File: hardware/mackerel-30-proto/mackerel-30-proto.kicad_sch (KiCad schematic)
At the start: 38 parts, among them J1 Conn_01x02, J2 Conn_01x02, J3 Conn_02x05_Odd_Even, U1 MC68030RC, U2 EPM7128, X1 CXO_DIP14

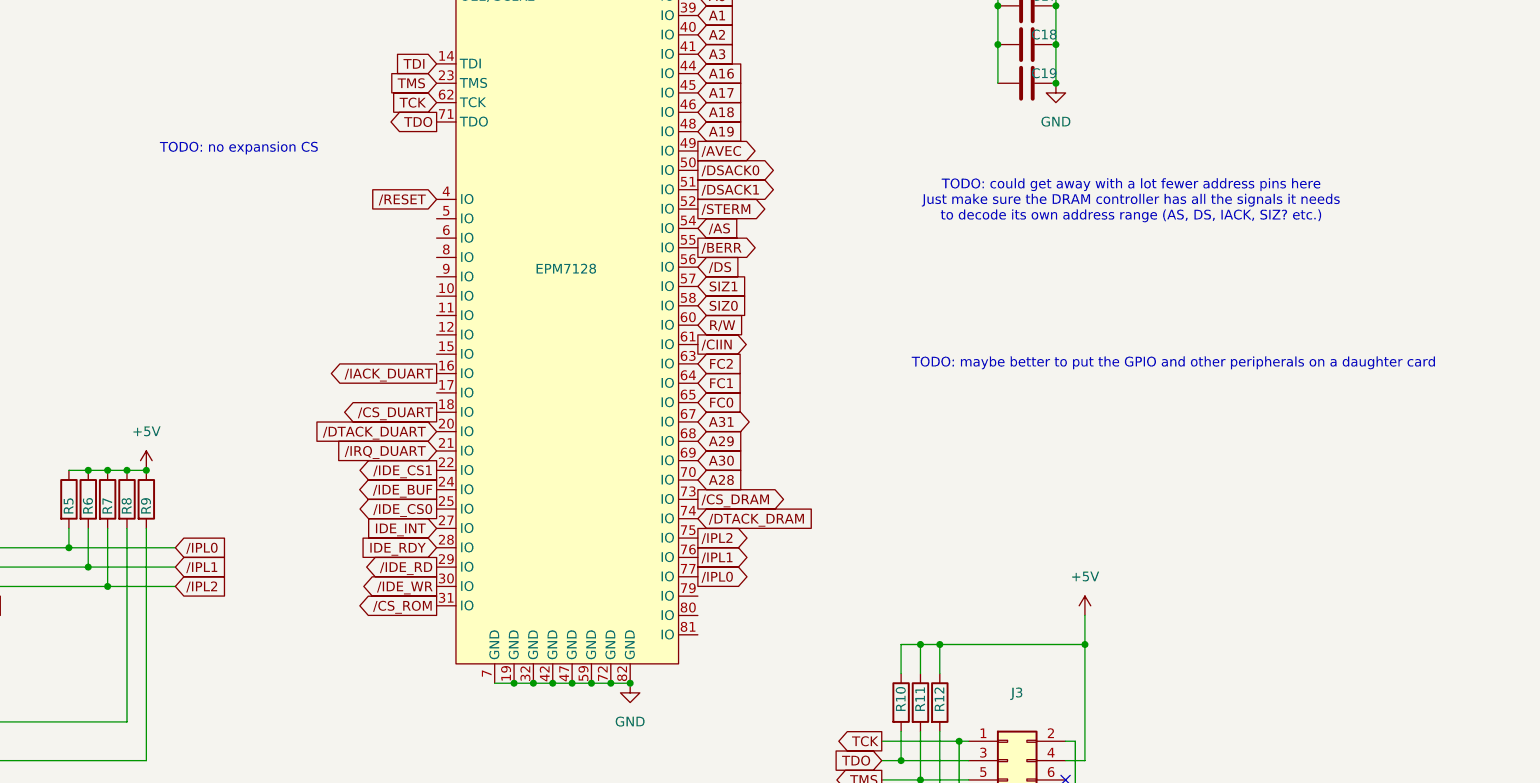
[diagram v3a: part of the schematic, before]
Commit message: Expansion header routed
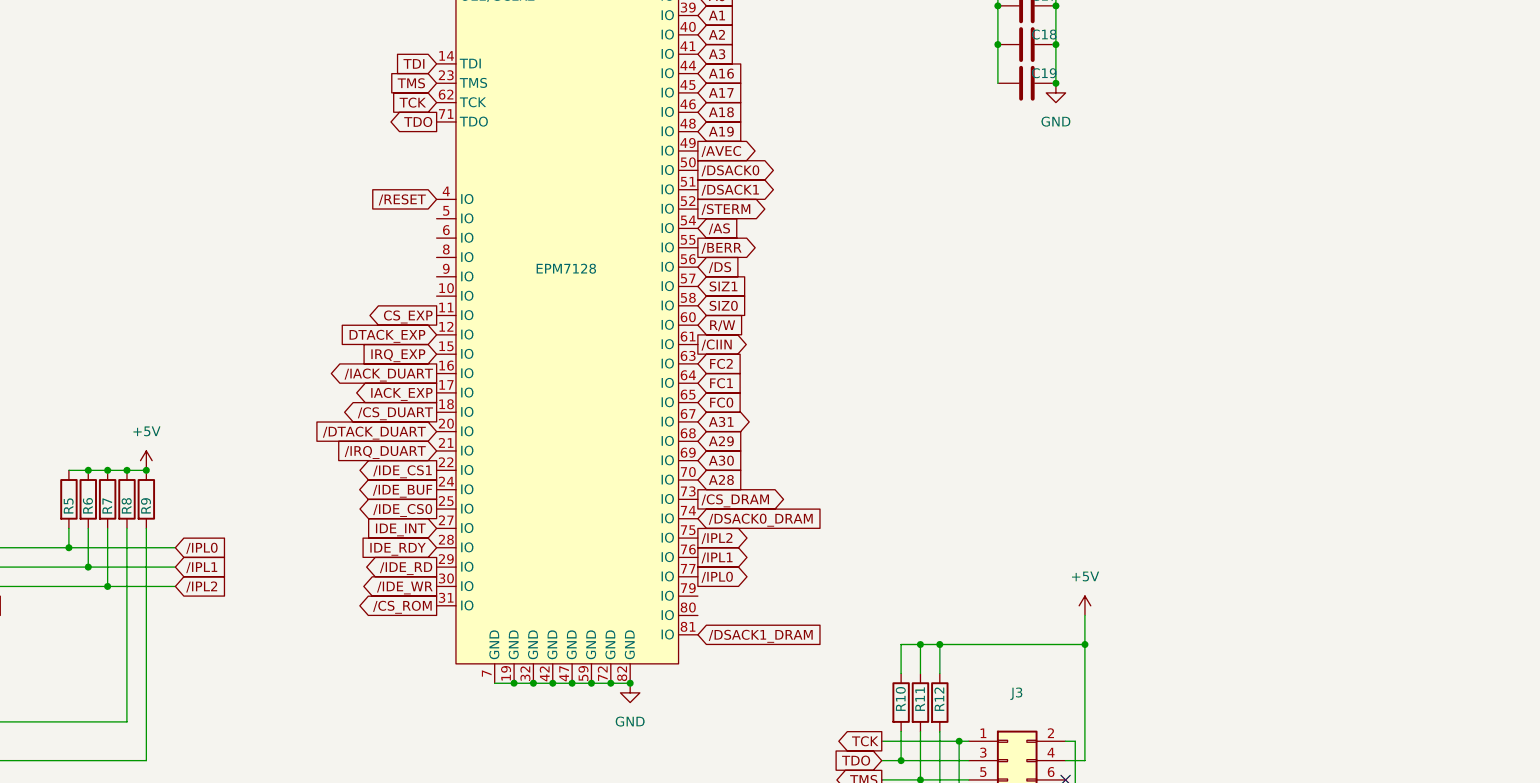
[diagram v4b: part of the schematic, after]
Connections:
- net CS_EXP: now reaches U2.11 (IO)
- net DTACK_EXP: now reaches U2.12 (IO)
- net IRQ_EXP: now reaches U2.15 (IO)
- net IACK_EXP: now reaches U2.17 (IO)
- net /DSACK1_DRAM: now reaches U2.81 (IO)
- net /DTACK_DRAM renamed /DSACK0_DRAM
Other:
- note removed: "TODO: could get away with a lot fewer address pins here Just make sure the DRAM controller has all the signals it needs to decode its own address range (AS, DS, IACK, SIZ? etc.)"
- note removed: "TODO: maybe better to put the GPIO and other peripherals on a daughter card"
- note removed: "TODO: no expansion CS"
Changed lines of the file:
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@@
-		)
-	)
-	(text "TODO: maybe better to put the GPIO and other peripherals on a daughter card"
-		(exclude_from_sim no)
-		(at 274.574 95.25 0)
-		(effects
-			(font
-				(size 1.27 1.27)
-			)
-		)
-	)
-	(text "TODO: no expansion CS"
-		(exclude_from_sim no)
-		(at 151.892 67.056 0)
-		(effects
-			(font
-				(size 1.27 1.27)
-			)
-		)
-	)
-	(text "TODO: could get away with a lot fewer address pins here\nJust make sure the DRAM controller has all the signals it needs\nto decode its own address range (AS, DS, IACK, SIZ? etc.)"
-		(exclude_from_sim no)
-		(at 268.986 73.914 0)
-		(effects
-			(font
-				(size 1.27 1.27)
-			)
 		)
 	)
@@
 		)
 	)
+	(global_label "{slash}DSACK1_DRAM"
+		(shape input)
+		(at 212.09 130.81 0)
+		(fields_autoplaced yes)
+		(effects
+			(font
+				(size 1.27 1.27)
+			)
+			(justify left)
+		)
+		(property "Intersheetrefs" "${INTERSHEET_REFS}"
+			(at 229.7709 130.81 0)
+			(effects
+				(font
+					(size 1.27 1.27)
+				)
+				(justify left)
+				(hide yes)
+			)
+		)
+	)
 	(global_label "{slash}IPL0"
 		(shape output)
@@
 		)
 	)
+	(global_label "DTACK_EXP"
+		(shape input)
+		(at 177.8 91.44 180)
+		(fields_autoplaced yes)
+		(effects
+			(font
+				(size 1.27 1.27)
+			)
+			(justify right)
+		)
+		(property "Intersheetrefs" "${INTERSHEET_REFS}"
+			(at 164.3525 91.44 0)
+			(effects
+				(font
+					(size 1.27 1.27)
+				)
+				(justify right)
+				(hide yes)
+			)
+		)
+	)
 	(global_label "{slash}CS_ROM"
 		(shape output)
@@
 		)
 	)
+	(global_label "IRQ_EXP"
+		(shape input)
+		(at 177.8 93.98 180)
+		(fields_autoplaced yes)
+		(effects
+			(font
+				(size 1.27 1.27)
+			)
+			(justify right)
+		)
+		(property "Intersheetrefs" "${INTERSHEET_REFS}"
+			(at 167.0134 93.98 0)
+			(effects
+				(font
+					(size 1.27 1.27)
+				)
+				(justify right)
+				(hide yes)
+			)
+		)
+	)
 	(global_label "FC2"
 		(shape output)
@@
 		)
 	)
-	(global_label "{slash}DTACK_DRAM"
+	(global_label "{slash}DSACK0_DRAM"
 		(shape input)
 		(at 212.09 115.57 0)
@@
 		)
 		(property "Intersheetrefs" "${INTERSHEET_REFS}"
-			(at 228.3195 115.57 0)
+			(at 229.7709 115.57 0)
 			(effects
 				(font
@@
 		)
 	)
+	(global_label "IACK_EXP"
+		(shape output)
+		(at 177.8 99.06 180)
+		(fields_autoplaced yes)
+		(effects
+			(font
+				(size 1.27 1.27)
+			)
+			(justify right)
+		)
+		(property "Intersheetrefs" "${INTERSHEET_REFS}"
+			(at 165.9853 99.06 0)
+			(effects
+				(font
+					(size 1.27 1.27)
+				)
+				(justify right)
+				(hide yes)
+			)
+		)
+	)
 	(global_label "D29"
 		(shape bidirectional)
@@
 			(effects
 				(font
+					(size 1.27 1.27)
+				)
+				(justify right)
+				(hide yes)
+			)
+		)
+	)
+	(global_label "CS_EXP"
+		(shape output)
+		(at 177.8 88.9 180)
+		(fields_autoplaced yes)
+		(effects
+			(font
+				(size 1.27 1.27)
+			)
+			(justify right)
+		)
+		(property "Intersheetrefs" "${INTERSHEET_REFS}"
+			(at 167.7392 88.9 0)
+			(effects
+				(font

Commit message: PCB cleanup
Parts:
- added J15: Conn_01x05, Connector_PinHeader_2.54mm:PinHeader_1x05_P2.54mm_Vertical, symbol Connector_Generic:Conn_01x05
- added R28, R29: 4k7, Resistor_THT:R_Axial_DIN0207_L6.3mm_D2.5mm_P7.62mm_Horizontal, symbol Device:R
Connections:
- net +5V: now also R28.2, R29.2
- net DTACK_EXP: now also R28.1
- net GND: now also U2.1 (GCLRn), U2.84 (OE1)
- net IRQ_EXP: now also R29.1
- net at U2.10 (IO): now also J15.5 (Pin_5)
- net at U2.5 (IO): now also J15.1 (Pin_1)
- net at U2.6 (IO): now also J15.2 (Pin_2)
- net /EXP_BUF: now reaches U2.79 (IO)
- net at U2.8 (IO): now also J15.3 (Pin_3)
- net at U2.9 (IO): now also J15.4 (Pin_4)
- no-connect marks 14 -> 16
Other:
- title: Mackerel-30 Proto -> Mackerel-30
- moved on the sheet: C12, C13, C14, C15, C16, C17, C18, C19, X1

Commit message: Mackerel-30 v0.1 PCB release
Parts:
- R10, R11, R12, R13: value R -> 4k7
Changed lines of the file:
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@@
 			)
 		)
-		(property "Value" "R"
+		(property "Value" "4k7"
 			(at 241.3 140.9699 0)
 			(effects
@@
 			)
 		)
-		(property "Value" "R"
+		(property "Value" "4k7"
 			(at 246.38 140.9699 0)
 			(effects
@@
 			)
 		)
-		(property "Value" "R"
+		(property "Value" "4k7"
 			(at 243.84 140.9699 0)
 			(effects
@@
 			)
 		)
-		(property "Value" "R"
+		(property "Value" "4k7"
 			(at 248.92 161.2899 0)
 			(effects
